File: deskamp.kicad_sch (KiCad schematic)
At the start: 29 parts, among them J1 Input 01, J2 Input 02, J3 Preamp Out, J4 Selector Switch, J5 LFE, J6 Mute, J7 Sleep, J8 Motor, J9 Power, K1 TQ2-12V, K2 TQ2-12V, K3 TQ2-12V, K4 TQ2-12V, Q1 PN2222A, Q2 PN2222A, Q3 PN2222A, Q4 PN2222A, U1 esp32-wemos-d1-mini, U2 L9110, U3 TSR_1-2433

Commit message: Use Alps RK27 as temp
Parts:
- RV1: footprint (none) -> Potentiometer_THT:Potentiometer_Alps_RK163_Dual_Horizontal
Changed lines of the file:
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@@
 			)
 		)
-		(property "Footprint" ""
+		(property "Footprint" "Potentiometer_THT:Potentiometer_Alps_RK163_Dual_Horizontal"
 			(at 212.09 69.215 0)
 			(effects

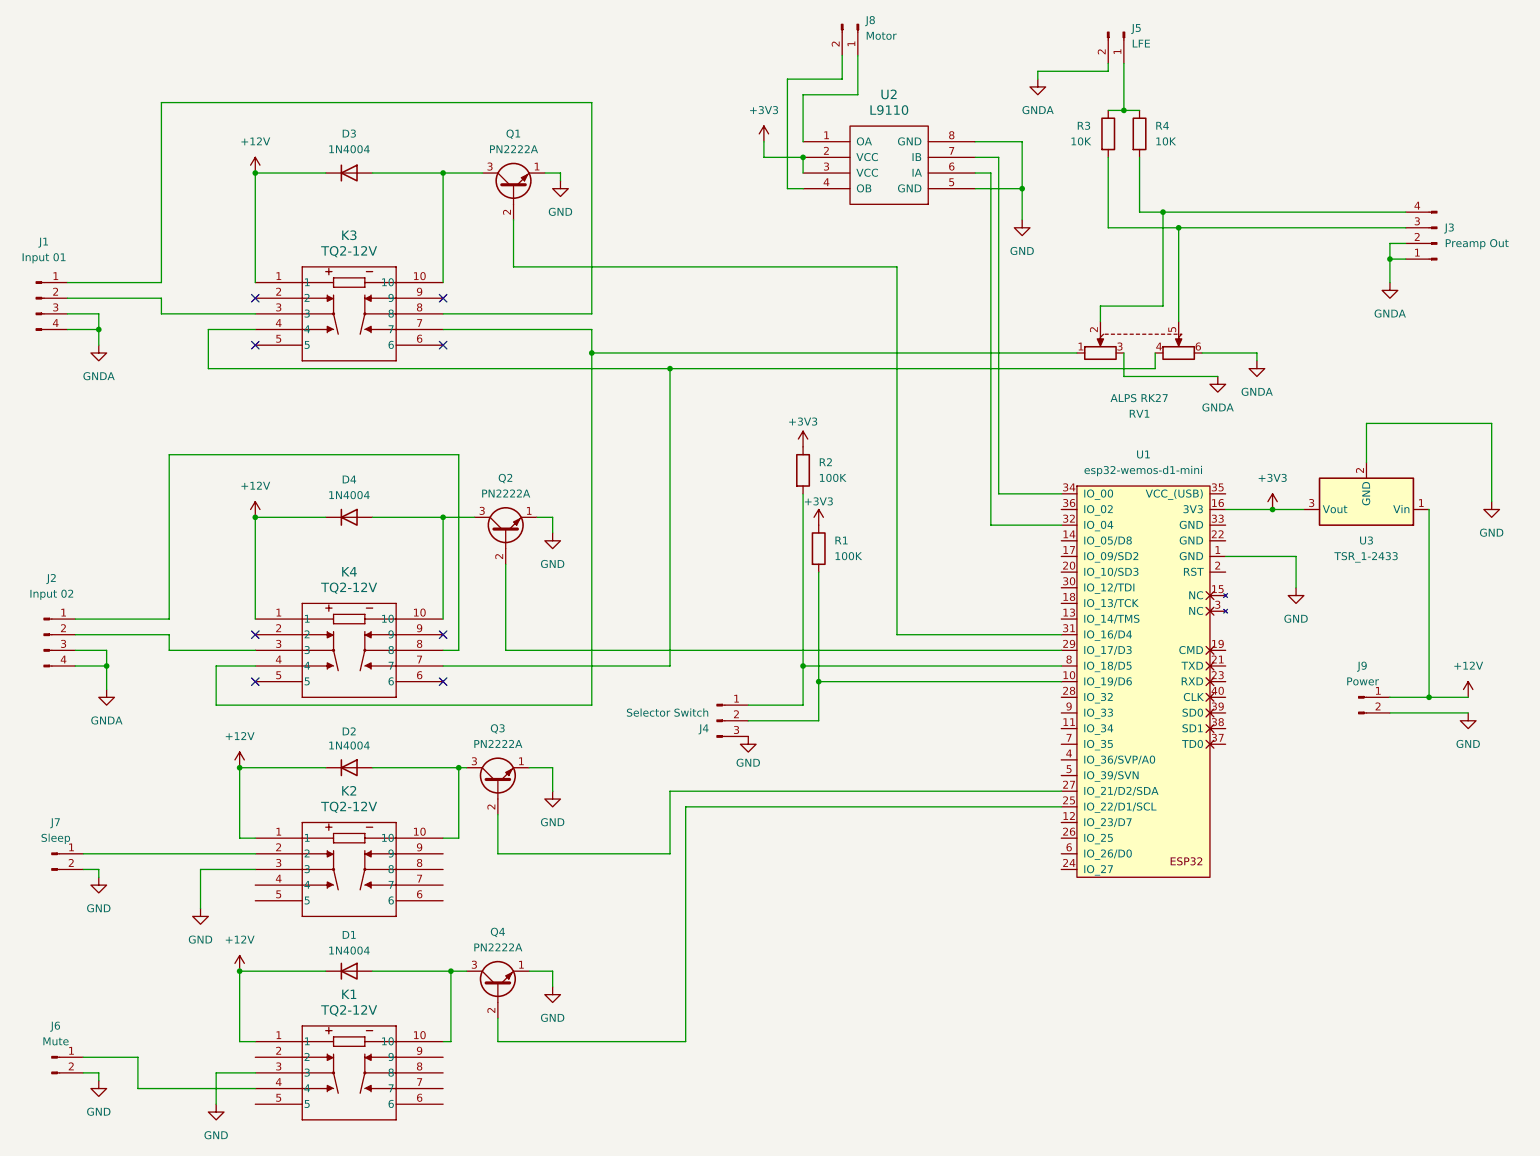
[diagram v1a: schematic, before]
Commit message: Add base resistors
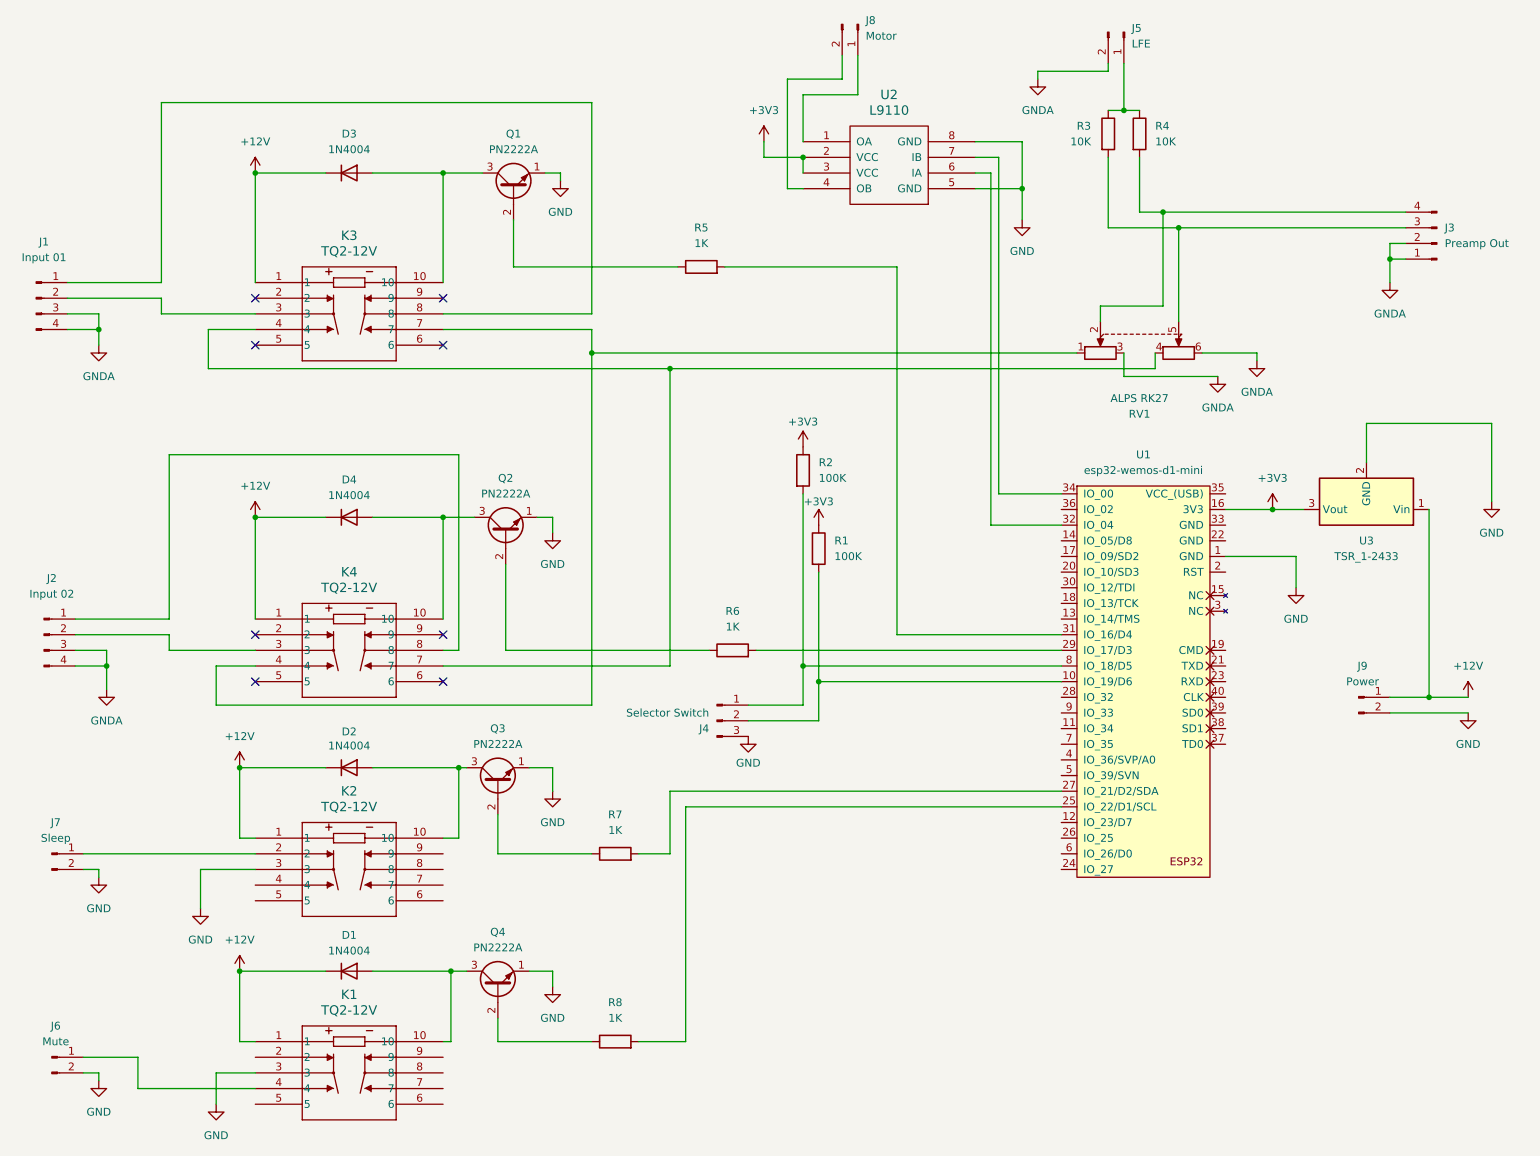
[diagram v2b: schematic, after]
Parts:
- added R5: 1K, Resistor_THT:R_Axial_DIN0204_L3.6mm_D1.6mm_P5.08mm_Horizontal, symbol Device:R
- added R6, R7, R8: 1K, symbol Device:R
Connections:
- net at Q3.2 (B): now also R7.1; no longer U1.27 (IO_21/D2/SDA)
- net at Q4.2 (B): now also R8.1; no longer U1.25 (IO_22/D1/SCL)
- net at Q2.2 (B): now also R6.1; no longer U1.29 (IO_17/D3)
- net at Q1.2 (B): now also R5.1; no longer U1.31 (IO_16/D4)
- new net: R8.2, U1.25 (IO_22/D1/SCL)
- new net: R6.2, U1.29 (IO_17/D3)
- new net: R5.2, U1.31 (IO_16/D4)
- new net: R7.2, U1.27 (IO_21/D2/SDA)

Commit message: Fix footprints
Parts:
- R6, R7, R8: footprint (none) -> Resistor_THT:R_Axial_DIN0204_L3.6mm_D1.6mm_P5.08mm_Horizontal
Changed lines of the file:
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@@
 			)
 		)
-		(property "Footprint" ""
+		(property "Footprint" "Resistor_THT:R_Axial_DIN0204_L3.6mm_D1.6mm_P5.08mm_Horizontal"
 			(at 120.65 183.388 90)
 			(effects
@@
 			)
 		)
-		(property "Footprint" ""
+		(property "Footprint" "Resistor_THT:R_Axial_DIN0204_L3.6mm_D1.6mm_P5.08mm_Horizontal"
 			(at 139.7 119.888 90)
 			(effects
@@
 			)
 		)
-		(property "Footprint" ""
+		(property "Footprint" "Resistor_THT:R_Axial_DIN0204_L3.6mm_D1.6mm_P5.08mm_Horizontal"
 			(at 120.65 152.908 90)
 			(effects

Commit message: Check footprints
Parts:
- R3, R4: footprint OptoDevice:R_LDR_5.2x5.2mm_P3.5mm_Horizontal -> Resistor_THT:R_Axial_Power_L38.0mm_W9.0mm_P40.64mm
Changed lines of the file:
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@@
 			)
 		)
-		(property "Footprint" "OptoDevice:R_LDR_5.2x5.2mm_P3.5mm_Horizontal"
+		(property "Footprint" "Resistor_THT:R_Axial_Power_L38.0mm_W9.0mm_P40.64mm"
 			(at 198.882 34.29 90)
 			(effects
@@
 			)
 		)
-		(property "Footprint" "OptoDevice:R_LDR_5.2x5.2mm_P3.5mm_Horizontal"
+		(property "Footprint" "Resistor_THT:R_Axial_Power_L38.0mm_W9.0mm_P40.64mm"
 			(at 203.962 34.29 90)
 			(effects

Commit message: Add rough pot footprint (first footprint!)
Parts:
- J6, J7: footprint Connector_JST:JST_XH_B2B-XH-A_1x02_P2.50mm_Vertical -> Connector_JST:JST_XH_B2B-XH-AM_1x02_P2.50mm_Vertical
- RV1: footprint Potentiometer_THT:Potentiometer_Alps_RK163_Dual_Horizontal -> Potentiometer_THT:Potentiometer_Alps_RK27112MC
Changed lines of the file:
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@@
 			)
 		)
-		(property "Footprint" "Connector_JST:JST_XH_B2B-XH-A_1x02_P2.50mm_Vertical"
+		(property "Footprint" "Connector_JST:JST_XH_B2B-XH-AM_1x02_P2.50mm_Vertical"
 			(at 29.21 184.15 0)
 			(effects
@@
 			)
 		)
-		(property "Footprint" "Connector_JST:JST_XH_B2B-XH-A_1x02_P2.50mm_Vertical"
+		(property "Footprint" "Connector_JST:JST_XH_B2B-XH-AM_1x02_P2.50mm_Vertical"
 			(at 29.21 151.13 0)
 			(effects
@@
 			)
 		)
-		(property "Footprint" "Potentiometer_THT:Potentiometer_Alps_RK163_Dual_Horizontal"
+		(property "Footprint" "Potentiometer_THT:Potentiometer_Alps_RK27112MC"
 			(at 212.09 69.215 0)
 			(effects

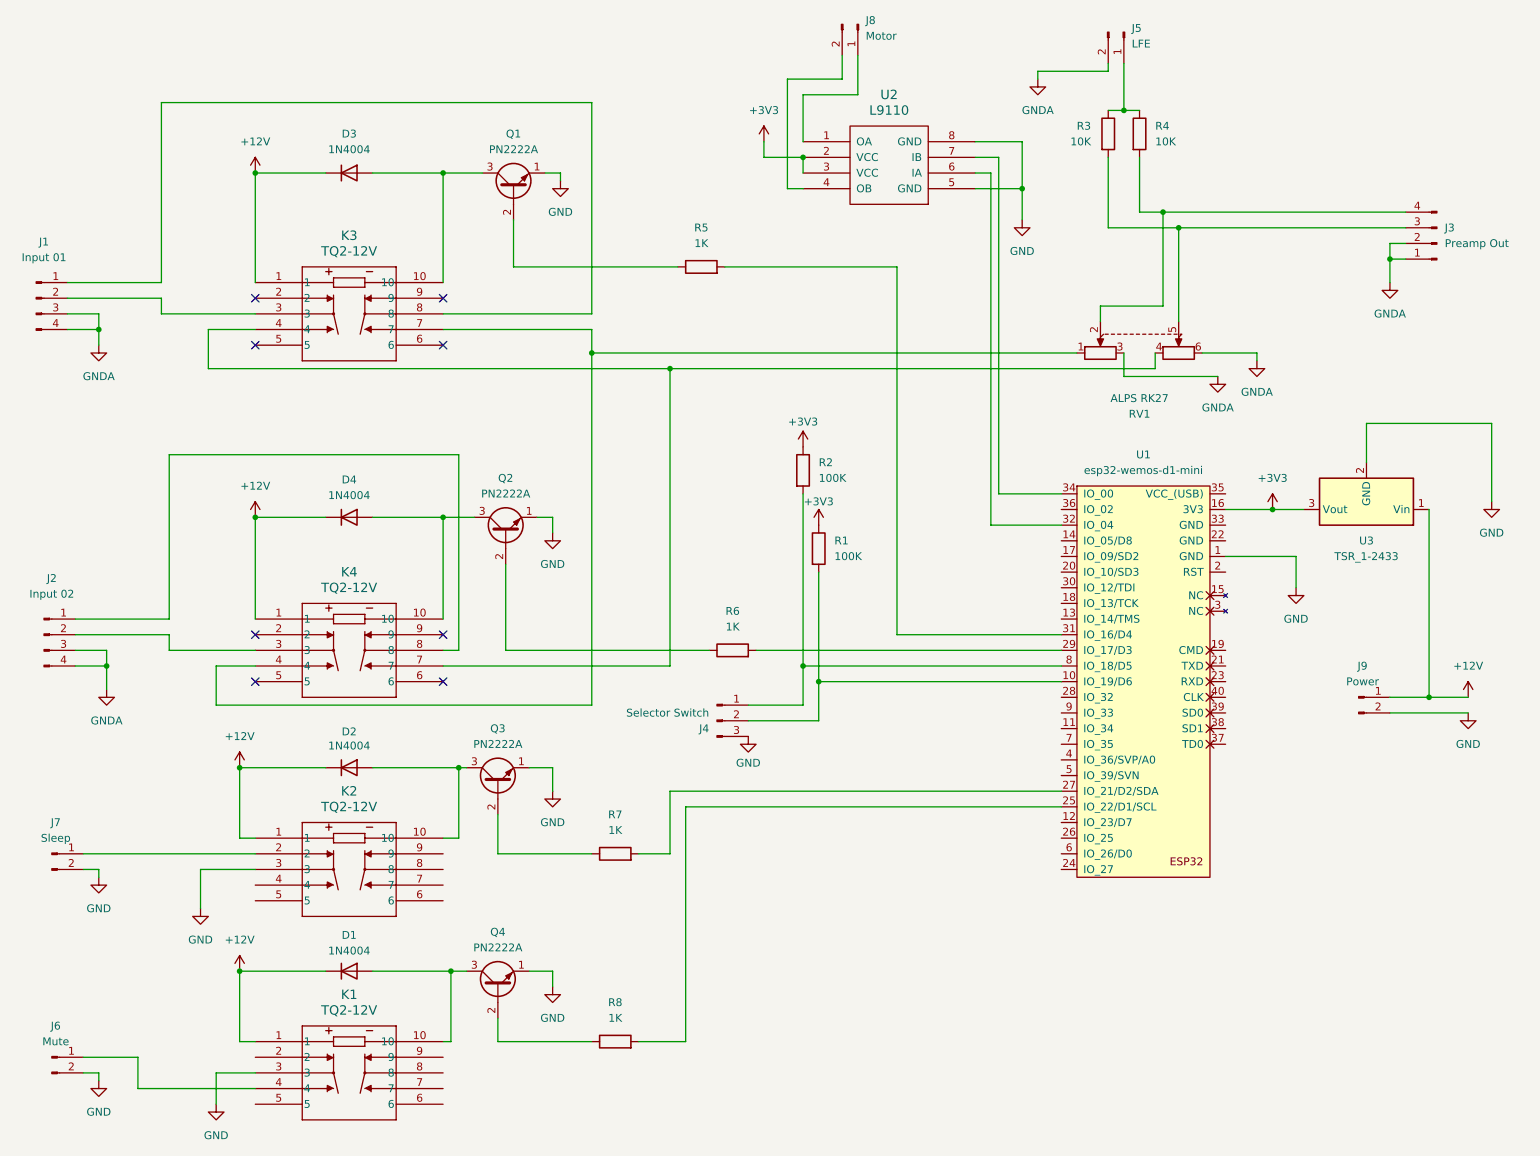
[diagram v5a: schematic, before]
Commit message: Add NC tags to pass ERC
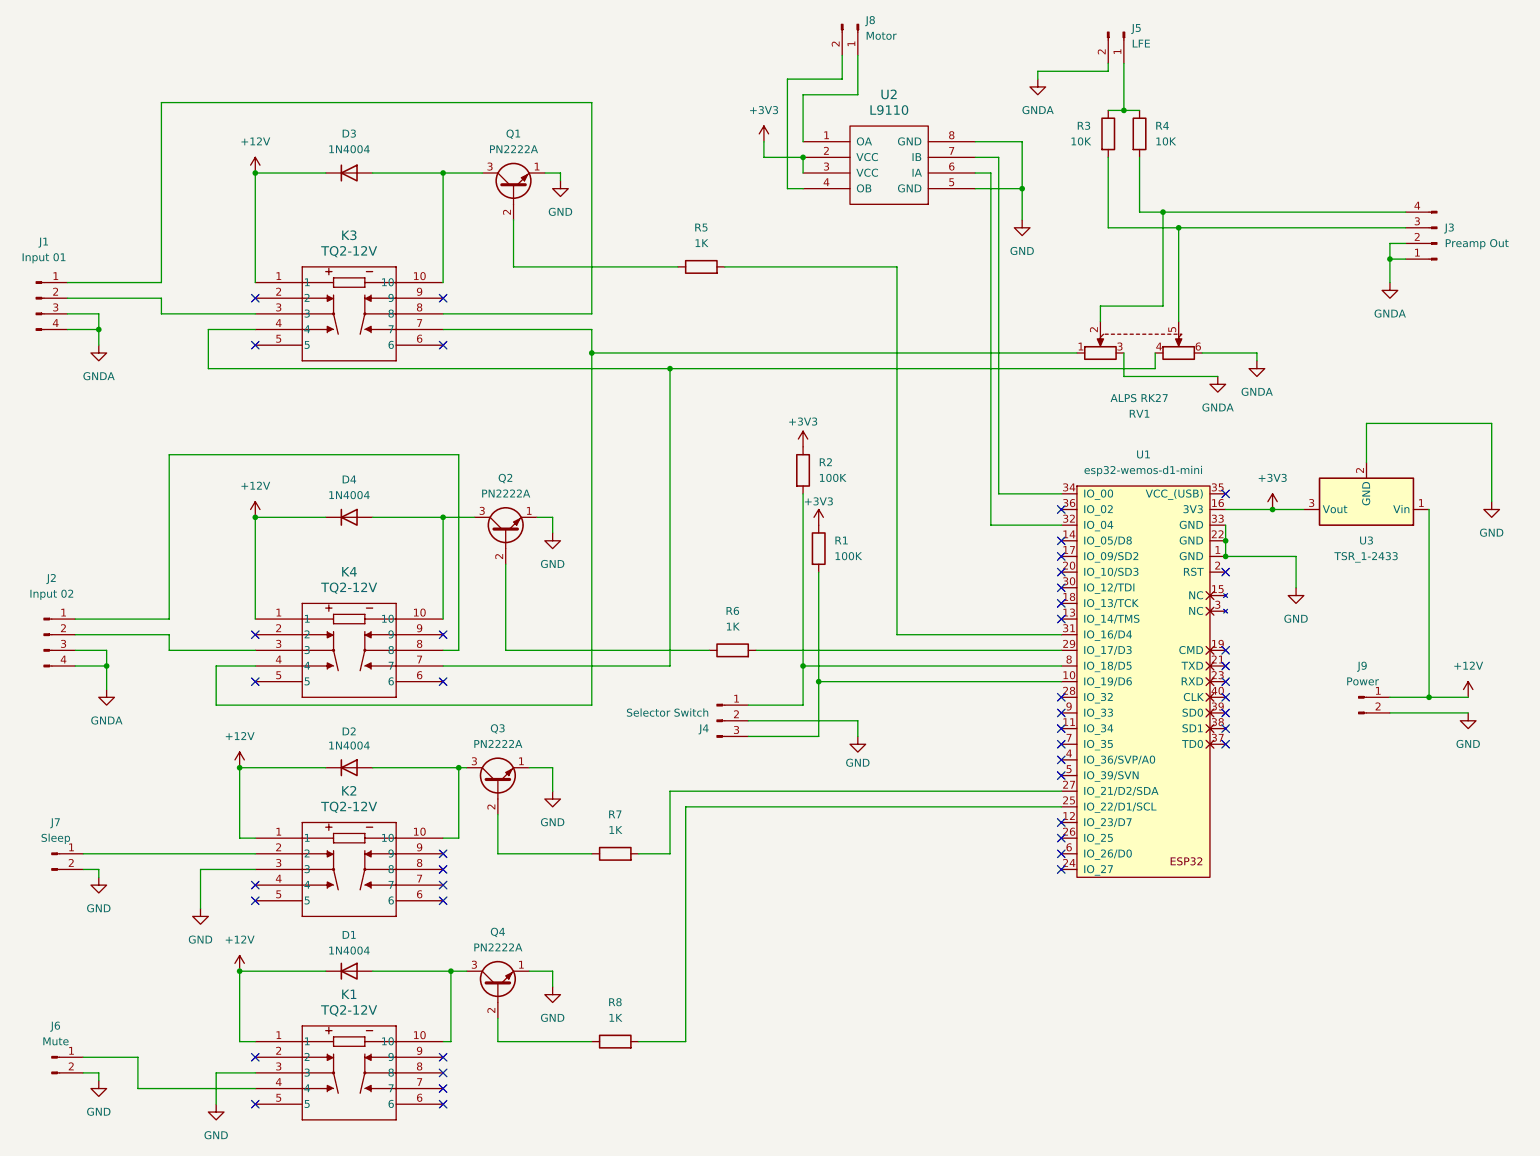
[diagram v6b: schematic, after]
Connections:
- net GND: now also J4.2 (Pin_2), U1.22 (GND), U1.33 (GND); no longer J4.3 (Pin_3)
- net at R1.2, U1.10 (IO_19/D6): now also J4.3 (Pin_3); no longer J4.2 (Pin_2)
- no-connect marks 8 -> 46
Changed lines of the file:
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@@
 	)
 	(junction
+		(at 219.71 100.33)
+		(diameter 0)
+		(color 0 0 0 0)
+	)
+	(junction
 		(at 203.2 30.48)
 		(diameter 0)
@@
 	)
 	(junction
+		(at 219.71 102.87)
+		(diameter 0)
+		(color 0 0 0 0)
+	)
+	(junction
 		(at 186.69 43.18)
 		(diameter 0)
@@
 	)
 	(no_connect
+		(at 193.04 128.27)
+	)
+	(no_connect
 		(at 92.71 60.96)
 	)
 	(no_connect
+		(at 92.71 186.69)
+	)
+	(no_connect
+		(at 193.04 151.13)
+	)
+	(no_connect
+		(at 193.04 95.25)
+	)
+	(no_connect
 		(at 92.71 115.57)
 	)
 	(no_connect
+		(at 193.04 133.35)
+	)
+	(no_connect
+		(at 92.71 189.23)
+	)
+	(no_connect
+		(at 193.04 125.73)
+	)
+	(no_connect
+		(at 193.04 153.67)
+	)
+	(no_connect
+		(at 92.71 156.21)
+	)
+	(no_connect
+		(at 62.23 191.77)
+	)
+	(no_connect
+		(at 219.71 130.81)
+	)
+	(no_connect
 		(at 62.23 68.58)
 	)
 	(no_connect
+		(at 219.71 123.19)
+	)
+	(no_connect
+		(at 219.71 105.41)
+	)
+	(no_connect
+		(at 193.04 107.95)
+	)
+	(no_connect
+		(at 193.04 100.33)
+	)
+	(no_connect
+		(at 62.23 184.15)
+	)
+	(no_connect
+		(at 193.04 105.41)
+	)
+	(no_connect
+		(at 193.04 148.59)
+	)
+	(no_connect
+		(at 219.71 92.71)
+	)
+	(no_connect
+		(at 92.71 151.13)
+	)
+	(no_connect
+		(at 92.71 158.75)
+	)
+	(no_connect
+		(at 193.04 146.05)
+	)
+	(no_connect
+		(at 219.71 133.35)
+	)
+	(no_connect
+		(at 193.04 110.49)
+	)
+	(no_connect
 		(at 62.23 123.19)
 	)
 	(no_connect
+		(at 219.71 118.11)
+	)
+	(no_connect
+		(at 193.04 113.03)
+	)
+	(no_connect
+		(at 193.04 102.87)
+	)
+	(no_connect
+		(at 219.71 125.73)
+	)
+	(no_connect
+		(at 219.71 128.27)
+	)
+	(no_connect
+		(at 92.71 153.67)
+	)
+	(no_connect
+		(at 62.23 158.75)
+	)
+	(no_connect
+		(at 219.71 120.65)
+	)
+	(no_connect
 		(at 92.71 68.58)
 	)
 	(no_connect
+		(at 193.04 130.81)
+	)
+	(no_connect
+		(at 92.71 184.15)
+	)
+	(no_connect
 		(at 92.71 123.19)
 	)
@@
 		(at 62.23 115.57)
 	)
+	(no_connect
+		(at 62.23 156.21)
+	)
+	(no_connect
+		(at 193.04 138.43)
+	)
+	(no_connect
+		(at 193.04 135.89)
+	)
+	(no_connect
+		(at 92.71 191.77)
+	)
 	(wire
 		(pts
@@
 	(wire
 		(pts
+			(xy 142.24 132.08) (xy 153.67 132.08)
+		)
+		(stroke
+			(width 0)
+			(type default)
+		)
+	)
+	(wire
+		(pts
 			(xy 81.28 137.16) (xy 95.25 137.16)
 		)
@@
 	(wire
 		(pts
+			(xy 219.71 97.79) (xy 219.71 100.33)
+		)
+		(stroke
+			(width 0)
+			(type default)
+		)
+	)
+	(wire
+		(pts
 			(xy 34.29 151.13) (xy 62.23 151.13)
 		)
@@
 	(wire
 		(pts
-			(xy 153.67 123.19) (xy 153.67 129.54)
+			(xy 153.67 123.19) (xy 153.67 132.08)
 		)
 		(stroke
@@
 	(wire
 		(pts
+			(xy 160.02 129.54) (xy 142.24 129.54)
+		)
+		(stroke
+			(width 0)
+			(type default)
+		)
+	)
+	(wire
+		(pts
 			(xy 34.29 184.15) (xy 43.18 184.15)
 		)
@@
 	(wire
 		(pts
-			(xy 36.83 63.5) (xy 36.83 66.04)
+			(xy 219.71 100.33) (xy 219.71 102.87)
 		)
 		(stroke
@@
 	(wire
 		(pts
-			(xy 95.25 137.16) (xy 96.52 137.16)
+			(xy 36.83 63.5) (xy 36.83 66.04)
 		)
 		(stroke
@@
 	(wire
 		(pts
-			(xy 116.84 63.5) (xy 92.71 63.5)
+			(xy 95.25 137.16) (xy 96.52 137.16)
 		)
 		(stroke
@@
 	(wire
 		(pts
-			(xy 153.67 129.54) (xy 142.24 129.54)
+			(xy 116.84 63.5) (xy 92.71 63.5)
 		)
 		(stroke
@@
 	(wire
 		(pts
+			(xy 160.02 132.08) (xy 160.02 129.54)
+		)
+		(stroke
+			(width 0)
+			(type default)
+		)
+	)
+	(wire
+		(pts
 			(xy 62.23 153.67) (xy 53.34 153.67)
 		)
@@
 	(symbol
 		(lib_id "power:GND")
-		(at 142.24 132.08 0)
+		(at 160.02 132.08 0)
 		(unit 1)
 		(exclude_from_sim no)
@@
 		(dnp no)
 		(property "Reference" "#PWR010"
-			(at 142.24 138.43 0)
+			(at 160.02 138.43 0)
 			(effects
 				(font
@@
 		)
 		(property "Value" "GND"
-			(at 142.24 136.398 0)
+			(at 160.02 136.398 0)
 			(effects
 				(font
@@
 		)
 		(property "Footprint" ""
-			(at 142.24 132.08 0)
+			(at 160.02 132.08 0)
 			(effects
 				(font
@@
 		)
 		(property "Datasheet" ""
-			(at 142.24 132.08 0)
+			(at 160.02 132.08 0)
 			(effects
 				(font
@@
 		)
 		(property "Description" "Power symbol creates a global label with name \"GND\" , ground"
-			(at 142.24 132.08 0)
+			(at 160.02 132.08 0)
 			(effects
 				(font
